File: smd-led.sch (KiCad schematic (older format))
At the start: 26 parts, among them Q14 Q_NPN_BEC, Q15 Q_NPN_BEC, Q17 Q_NPN_BEC, Q18 Q_NPN_BEC

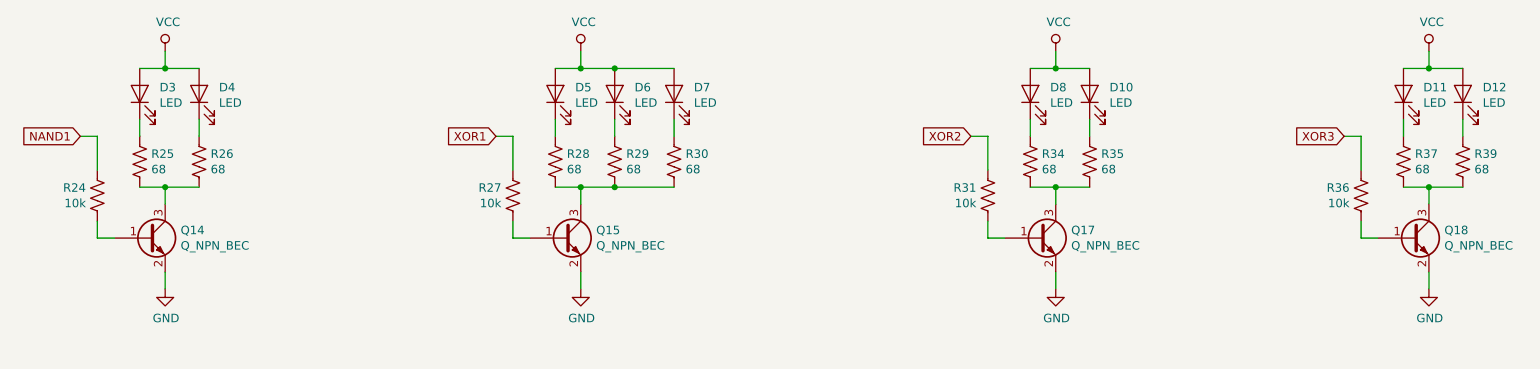
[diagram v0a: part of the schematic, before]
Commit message: refactor numeric assignments
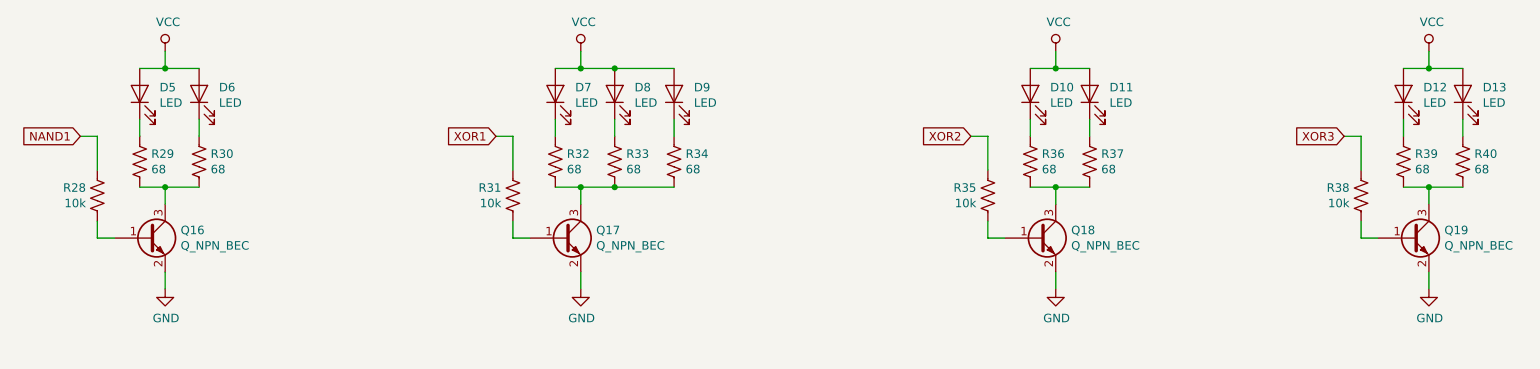
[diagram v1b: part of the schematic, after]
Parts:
- renumbered D8 to D10, D10 to D11, D11 to D12, D12 to D13, D3 to D5, D4 to D6, D5 to D7, D6 to D8, D7 to D9, Q14 to Q16, Q15 to Q17, Q17 to Q18, Q18 to Q19, R24 to R28, R25 to R29, R26 to R30, R27 to R31, R28 to R32, R29 to R33, R30 to R34, R31 to R35, R34 to R36, R35 to R37, R36 to R38, R37 to R39, R39 to R40
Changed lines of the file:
@@
 $EndDescr
 $Comp
-L Device:LED D3
+L Device:LED D5
 U 1 1 5CFFBE87
 P 1950 1500
-F 0 "D3" V 1988 1383 50  0000 R CNN
+F 0 "D5" V 1988 1383 50  0000 R CNN
 F 1 "LED" V 1897 1383 50  0000 R CNN
 F 2 "--Project:LED_1206_3216Metric_ReverseMount_Hole1.8x2.4mm" H 1950 1500 50  0001 C CNN
@@
 $EndComp
 $Comp
-L Device:R_US R25
+L Device:R_US R29
 U 1 1 5CFFBE8E
 P 1950 1900
-F 0 "R25" H 2018 1946 50  0000 L CNN
+F 0 "R29" H 2018 1946 50  0000 L CNN
 F 1 "68" H 2018 1855 50  0000 L CNN
 F 2 "Resistor_SMD:R_0805_2012Metric_Pad1.15x1.40mm_HandSolder" V 1990 1890 50  0001 C CNN
@@
 $EndComp
 $Comp
-L power:GND #PWR02
+L power:GND #PWR028
 U 1 1 5CFFBE95
 P 2100 2650
-F 0 "#PWR02" H 2100 2400 50  0001 C CNN
+F 0 "#PWR028" H 2100 2400 50  0001 C CNN
 F 1 "GND" H 2105 2477 50  0000 C CNN
 F 2 "" H 2100 2650 50  0001 C CNN
@@
 	1950 1750 1950 1650
 $Comp
-L power:VCC #PWR01
+L power:VCC #PWR027
 U 1 1 5CFFBE9D
 P 2100 1250
-F 0 "#PWR01" H 2100 1100 50  0001 C CNN
+F 0 "#PWR027" H 2100 1100 50  0001 C CNN
 F 1 "VCC" H 2117 1423 50  0000 C CNN
 F 2 "" H 2100 1250 50  0001 C CNN
@@
 	2100 1250 2100 1350
 $Comp
-L Device:R_US R24
+L Device:R_US R28
 U 1 1 5CFFBEA4
 P 1700 2100
-F 0 "R24" H 1767 2054 50  0000 L CNN
+F 0 "R28" H 1767 2054 50  0000 L CNN
 F 1 "10k" H 1767 2145 50  0000 L CNN
 F 2 "Resistor_SMD:R_0805_2012Metric_Pad1.15x1.40mm_HandSolder" V 1740 2090 50  0001 C CNN
@@
 	1600 1750 1700 1750
 $Comp
-L Device:LED D4
+L Device:LED D6
 U 1 1 5CFFBEB2
 P 2300 1500
-F 0 "D4" V 2338 1383 50  0000 R CNN
+F 0 "D6" V 2338 1383 50  0000 R CNN
 F 1 "LED" V 2247 1383 50  0000 R CNN
 F 2 "--Project:LED_1206_3216Metric_ReverseMount_Hole1.8x2.4mm" H 2300 1500 50  0001 C CNN
@@
 $EndComp
 $Comp
-L Device:R_US R26
+L Device:R_US R30
 U 1 1 5CFFBEB9
 P 2300 1900
-F 0 "R26" H 2368 1946 50  0000 L CNN
+F 0 "R30" H 2368 1946 50  0000 L CNN
 F 1 "68" H 2368 1855 50  0000 L CNN
 F 2 "Resistor_SMD:R_0805_2012Metric_Pad1.15x1.40mm_HandSolder" V 2340 1890 50  0001 C CNN
@@
 	2100 1350 2300 1350
 $Comp
-L Device:LED D8
+L Device:LED D10
 U 1 1 5CFFBEC8
 P 7200 1500
-F 0 "D8" V 7238 1383 50  0000 R CNN
+F 0 "D10" V 7238 1383 50  0000 R CNN
 F 1 "LED" V 7147 1383 50  0000 R CNN
 F 2 "--Project:LED_1206_3216Metric_ReverseMount_Hole1.8x2.4mm" H 7200 1500 50  0001 C CNN
@@
 $EndComp
 $Comp
-L Device:R_US R34
+L Device:R_US R36
 U 1 1 5CFFBECF
 P 7200 1900
-F 0 "R34" H 7268 1946 50  0000 L CNN
+F 0 "R36" H 7268 1946 50  0000 L CNN
 F 1 "68" H 7268 1855 50  0000 L CNN
 F 2 "Resistor_SMD:R_0805_2012Metric_Pad1.15x1.40mm_HandSolder" V 7240 1890 50  0001 C CNN
@@
 $EndComp
 $Comp
-L power:GND #PWR07
+L power:GND #PWR032
 U 1 1 5CFFBED6
 P 7350 2650
-F 0 "#PWR07" H 7350 2400 50  0001 C CNN
+F 0 "#PWR032" H 7350 2400 50  0001 C CNN
 F 1 "GND" H 7355 2477 50  0000 C CNN
 F 2 "" H 7350 2650 50  0001 C CNN
@@
 	7200 1750 7200 1650
 $Comp
-L power:VCC #PWR06
+L power:VCC #PWR031
 U 1 1 5CFFBEDE
 P 7350 1250
-F 0 "#PWR06" H 7350 1100 50  0001 C CNN
+F 0 "#PWR031" H 7350 1100 50  0001 C CNN
 F 1 "VCC" H 7367 1423 50  0000 C CNN
 F 2 "" H 7350 1250 50  0001 C CNN
@@
 	7350 1250 7350 1350
 $Comp
-L Device:R_US R31
+L Device:R_US R35
 U 1 1 5CFFBEE5
 P 6950 2100
-F 0 "R31" H 7018 2054 50  0000 L CNN
+F 0 "R35" H 7018 2054 50  0000 L CNN
 F 1 "10k" H 7018 2145 50  0000 L CNN
 F 2 "Resistor_SMD:R_0805_2012Metric_Pad1.15x1.40mm_HandSolder" V 6990 2090 50  0001 C CNN
@@
 	6850 1750 6950 1750
 $Comp
-L Device:LED D10
+L Device:LED D11
 U 1 1 5CFFBEF3
 P 7550 1500
-F 0 "D10" V 7588 1383 50  0000 R CNN
+F 0 "D11" V 7588 1383 50  0000 R CNN
 F 1 "LED" V 7497 1383 50  0000 R CNN
 F 2 "--Project:LED_1206_3216Metric_ReverseMount_Hole1.8x2.4mm" H 7550 1500 50  0001 C CNN
@@
 $EndComp
 $Comp
-L Device:R_US R35
+L Device:R_US R37
 U 1 1 5CFFBEFA
 P 7550 1900
-F 0 "R35" H 7618 1946 50  0000 L CNN
+F 0 "R37" H 7618 1946 50  0000 L CNN
 F 1 "68" H 7618 1855 50  0000 L CNN
 F 2 "Resistor_SMD:R_0805_2012Metric_Pad1.15x1.40mm_HandSolder" V 7590 1890 50  0001 C CNN
@@
 	7350 1350 7550 1350
 $Comp
-L Device:LED D11
+L Device:LED D12
 U 1 1 5CFFBF09
 P 9400 1500
-F 0 "D11" V 9438 1383 50  0000 R CNN
+F 0 "D12" V 9438 1383 50  0000 R CNN
 F 1 "LED" V 9347 1383 50  0000 R CNN
 F 2 "--Project:LED_1206_3216Metric_ReverseMount_Hole1.8x2.4mm" H 9400 1500 50  0001 C CNN
@@
 $EndComp
 $Comp
-L Device:R_US R37
+L Device:R_US R39
 U 1 1 5CFFBF10
 P 9400 1900
-F 0 "R37" H 9468 1946 50  0000 L CNN
+F 0 "R39" H 9468 1946 50  0000 L CNN
 F 1 "68" H 9468 1855 50  0000 L CNN
 F 2 "Resistor_SMD:R_0805_2012Metric_Pad1.15x1.40mm_HandSolder" V 9440 1890 50  0001 C CNN
@@
 $EndComp
 $Comp
-L power:GND #PWR09
+L power:GND #PWR034
 U 1 1 5CFFBF17
 P 9550 2650
-F 0 "#PWR09" H 9550 2400 50  0001 C CNN
+F 0 "#PWR034" H 9550 2400 50  0001 C CNN
 F 1 "GND" H 9555 2477 50  0000 C CNN
 F 2 "" H 9550 2650 50  0001 C CNN
@@
 	9400 1750 9400 1650
 $Comp
-L power:VCC #PWR08
+L power:VCC #PWR033
 U 1 1 5CFFBF1F
 P 9550 1250
-F 0 "#PWR08" H 9550 1100 50  0001 C CNN
+F 0 "#PWR033" H 9550 1100 50  0001 C CNN
 F 1 "VCC" H 9567 1423 50  0000 C CNN
 F 2 "" H 9550 1250 50  0001 C CNN
@@
 	9550 1250 9550 1350
 $Comp
-L Device:R_US R36
+L Device:R_US R38
 U 1 1 5CFFBF26
 P 9150 2100
-F 0 "R36" H 9218 2054 50  0000 L CNN
+F 0 "R38" H 9218 2054 50  0000 L CNN
 F 1 "10k" H 9218 2145 50  0000 L CNN
 F 2 "Resistor_SMD:R_0805_2012Metric_Pad1.15x1.40mm_HandSolder" V 9190 2090 50  0001 C CNN
@@
 	9050 1750 9150 1750
 $Comp
-L Device:LED D12
+L Device:LED D13
 U 1 1 5CFFBF34
 P 9750 1500
-F 0 "D12" V 9788 1383 50  0000 R CNN
+F 0 "D13" V 9788 1383 50  0000 R CNN
 F 1 "LED" V 9697 1383 50  0000 R CNN
 F 2 "--Project:LED_1206_3216Metric_ReverseMount_Hole1.8x2.4mm" H 9750 1500 50  0001 C CNN
@@
 $EndComp
 $Comp
-L Device:R_US R39
+L Device:R_US R40
 U 1 1 5CFFBF3B
 P 9750 1900
-F 0 "R39" H 9818 1946 50  0000 L CNN
+F 0 "R40" H 9818 1946 50  0000 L CNN
 F 1 "68" H 9818 1855 50  0000 L CNN
 F 2 "Resistor_SMD:R_0805_2012Metric_Pad1.15x1.40mm_HandSolder" V 9790 1890 50  0001 C CNN
@@
 	9550 1350 9750 1350
 $Comp
-L Device:LED D5
+L Device:LED D7
 U 1 1 5CFFBF4A
 P 4400 1500
-F 0 "D5" V 4438 1383 50  0000 R CNN
+F 0 "D7" V 4438 1383 50  0000 R CNN
 F 1 "LED" V 4347 1383 50  0000 R CNN
 F 2 "--Project:LED_1206_3216Metric_ReverseMount_Hole1.8x2.4mm" H 4400 1500 50  0001 C CNN
@@
 $EndComp
 $Comp
-L Device:R_US R28
+L Device:R_US R32
 U 1 1 5CFFBF51
 P 4400 1900
-F 0 "R28" H 4468 1946 50  0000 L CNN
+F 0 "R32" H 4468 1946 50  0000 L CNN
 F 1 "68" H 4468 1855 50  0000 L CNN
 F 2 "Resistor_SMD:R_0805_2012Metric_Pad1.15x1.40mm_HandSolder" V 4440 1890 50  0001 C CNN
@@
 $EndComp
 $Comp
-L power:GND #PWR04
+L power:GND #PWR030
 U 1 1 5CFFBF58
 P 4550 2650
-F 0 "#PWR04" H 4550 2400 50  0001 C CNN
+F 0 "#PWR030" H 4550 2400 50  0001 C CNN
 F 1 "GND" H 4555 2477 50  0000 C CNN
 F 2 "" H 4550 2650 50  0001 C CNN
@@
 	4400 1750 4400 1650
 $Comp
-L power:VCC #PWR03
+L power:VCC #PWR029
 U 1 1 5CFFBF60
 P 4550 1250
-F 0 "#PWR03" H 4550 1100 50  0001 C CNN
+F 0 "#PWR029" H 4550 1100 50  0001 C CNN
 F 1 "VCC" H 4567 1423 50  0000 C CNN
 F 2 "" H 4550 1250 50  0001 C CNN
@@
 	4550 1250 4550 1350
 $Comp
-L Device:R_US R27
+L Device:R_US R31
 U 1 1 5CFFBF67
 P 4150 2100
-F 0 "R27" H 4218 2054 50  0000 L CNN
+F 0 "R31" H 4218 2054 50  0000 L CNN
 F 1 "10k" H 4218 2145 50  0000 L CNN
 F 2 "Resistor_SMD:R_0805_2012Metric_Pad1.15x1.40mm_HandSolder" V 4190 2090 50  0001 C CNN
@@
 	4050 1750 4150 1750
 $Comp
-L Device:LED D6
+L Device:LED D8
 U 1 1 5CFFBF75
 P 4750 1500
-F 0 "D6" V 4788 1383 50  0000 R CNN
+F 0 "D8" V 4788 1383 50  0000 R CNN
 F 1 "LED" V 4697 1383 50  0000 R CNN
 F 2 "--Project:LED_1206_3216Metric_ReverseMount_Hole1.8x2.4mm" H 4750 1500 50  0001 C CNN
@@
 $EndComp
 $Comp
-L Device:R_US R29
+L Device:R_US R33
 U 1 1 5CFFBF7C
 P 4750 1900
-F 0 "R29" H 4818 1946 50  0000 L CNN
+F 0 "R33" H 4818 1946 50  0000 L CNN
 F 1 "68" H 4818 1855 50  0000 L CNN
 F 2 "Resistor_SMD:R_0805_2012Metric_Pad1.15x1.40mm_HandSolder" V 4790 1890 50  0001 C CNN
@@
 	4750 1750 4750 1650
 $Comp
-L Device:LED D7
+L Device:LED D9
 U 1 1 5CFFBF85
 P 5100 1500
-F 0 "D7" V 5138 1383 50  0000 R CNN
+F 0 "D9" V 5138 1383 50  0000 R CNN
 F 1 "LED" V 5047 1383 50  0000 R CNN
 F 2 "--Project:LED_1206_3216Metric_ReverseMount_Hole1.8x2.4mm" H 5100 1500 50  0001 C CNN
@@
 $EndComp
 $Comp
-L Device:R_US R30
+L Device:R_US R34
 U 1 1 5CFFBF8C
 P 5100 1900
-F 0 "R30" H 5168 1946 50  0000 L CNN
+F 0 "R34" H 5168 1946 50  0000 L CNN
 F 1 "68" H 5168 1855 50  0000 L CNN
 F 2 "Resistor_SMD:R_0805_2012Metric_Pad1.15x1.40mm_HandSolder" V 5140 1890 50  0001 C CNN
@@
 	4750 1350 5100 1350
 $Comp
-L Device:Q_NPN_BEC Q14
+L Device:Q_NPN_BEC Q16
 U 1 1 5CFFBF9F
 P 2000 2350
-F 0 "Q14" H 2191 2396 50  0000 L CNN
+F 0 "Q16" H 2191 2396 50  0000 L CNN
 F 1 "Q_NPN_BEC" H 2191 2305 50  0000 L CNN
 F 2 "Package_TO_SOT_SMD:SOT-23_Handsoldering" H 2200 2450 50  0001 C CNN
@@
 $EndComp
 $Comp
-L Device:Q_NPN_BEC Q17
+L Device:Q_NPN_BEC Q18
 U 1 1 5CFFBFA7
 P 7250 2350
-F 0 "Q17" H 7441 2396 50  0000 L CNN
+F 0 "Q18" H 7441 2396 50  0000 L CNN
 F 1 "Q_NPN_BEC" H 7441 2305 50  0000 L CNN
 F 2 "Package_TO_SOT_SMD:SOT-23_Handsoldering" H 7450 2450 50  0001 C CNN
@@
 $EndComp
 $Comp
-L Device:Q_NPN_BEC Q18
+L Device:Q_NPN_BEC Q19
 U 1 1 5CFFBFAF
 P 9450 2350
-F 0 "Q18" H 9641 2396 50  0000 L CNN
+F 0 "Q19" H 9641 2396 50  0000 L CNN
 F 1 "Q_NPN_BEC" H 9641 2305 50  0000 L CNN
 F 2 "Package_TO_SOT_SMD:SOT-23_Handsoldering" H 9650 2450 50  0001 C CNN
@@
 $EndComp
 $Comp
-L Device:Q_NPN_BEC Q15
+L Device:Q_NPN_BEC Q17
 U 1 1 5CFFBFB7
 P 4450 2350
-F 0 "Q15" H 4641 2396 50  0000 L CNN
+F 0 "Q17" H 4641 2396 50  0000 L CNN
 F 1 "Q_NPN_BEC" H 4641 2305 50  0000 L CNN
 F 2 "Package_TO_SOT_SMD:SOT-23_Handsoldering" H 4650 2450 50  0001 C CNN

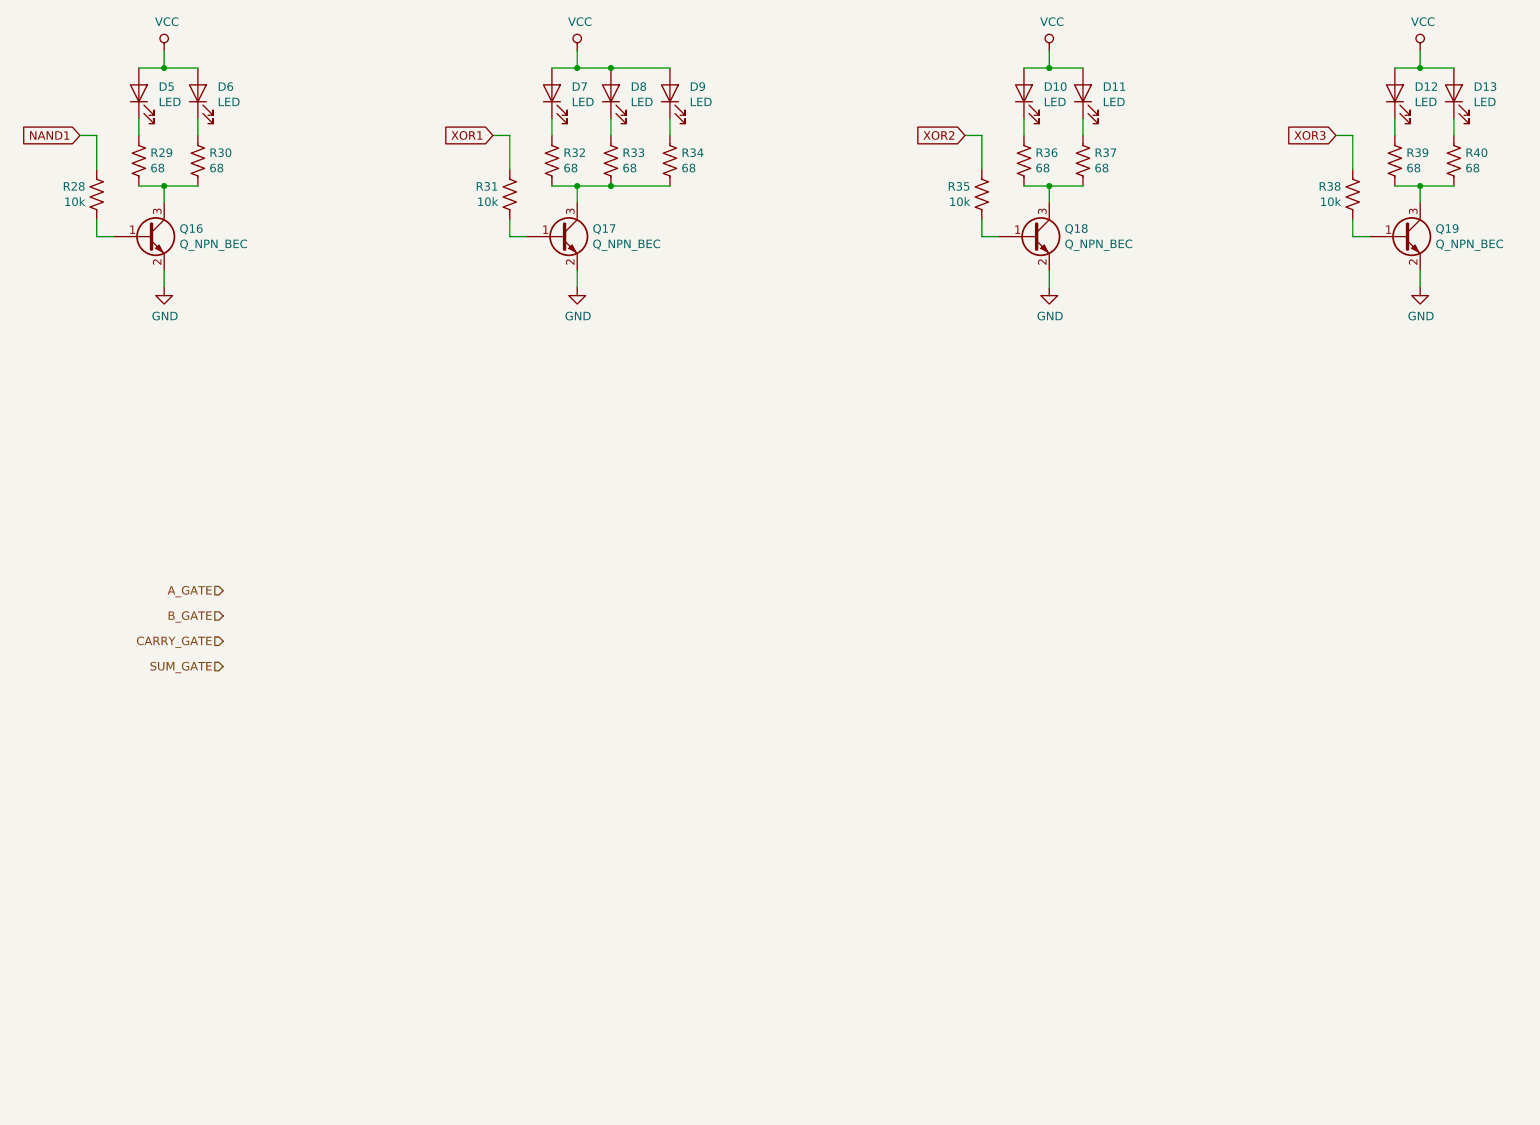
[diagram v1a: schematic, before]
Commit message: full smd led array layout done
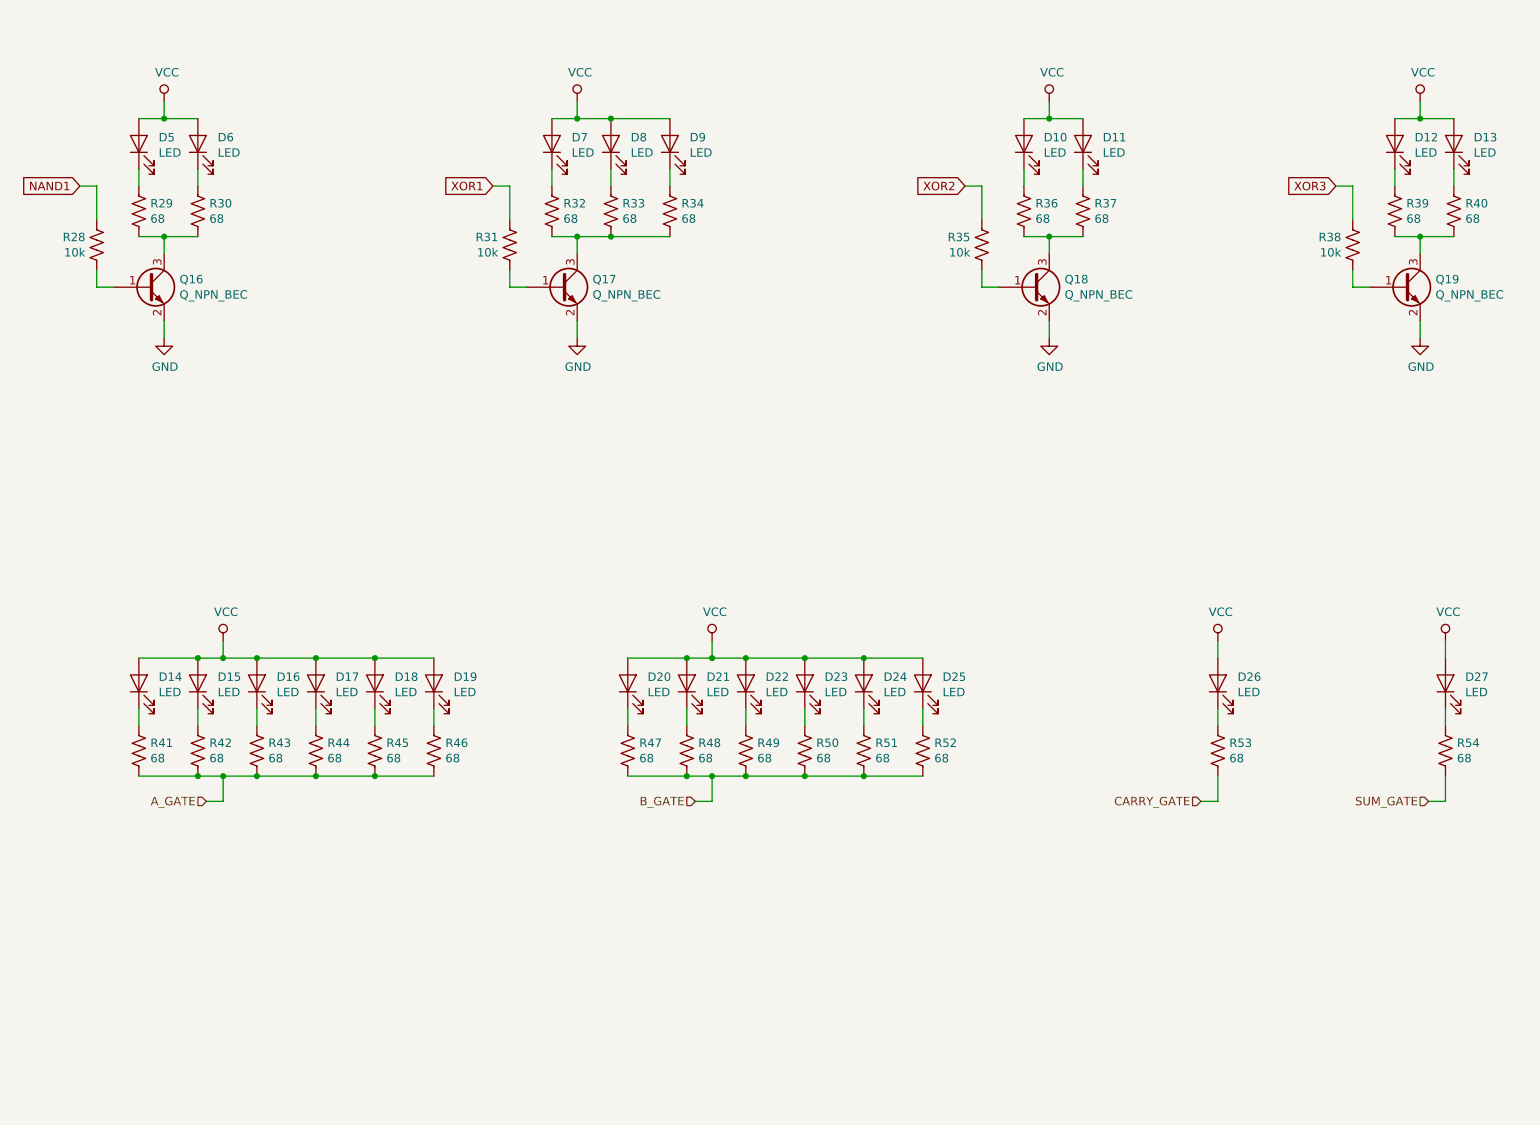
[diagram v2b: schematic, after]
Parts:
- added D14, D15, D16, D17, D18, D19, D20, D21, D22, D23, D24, D25, D26, D27: LED, --Project:LED_1206_3216Metric_ReverseMount_Hole1.8x2.4mm, symbol Device:LED
- added R41, R42, R43, R44, R45, R46, R47, R48, R49, R50, R51, R52, R53, R54: 68, Resistor_SMD:R_0805_2012Metric_Pad1.15x1.40mm_HandSolder, symbol Device:R_US
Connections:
- net A_GATE: now also R41.2, R42.2, R43.2, R44.2, R45.2, R46.2
- net B_GATE: now also R47.2, R48.2, R49.2, R50.2, R51.2, R52.2
- net CARRY_GATE: now also R53.2
- net SUM_GATE: now also R54.2
- net VCC: now also D14.2 (A), D15.2 (A), D16.2 (A), D17.2 (A), D18.2 (A), D19.2 (A), D20.2 (A), D21.2 (A), D22.2 (A), D23.2 (A), D24.2 (A), D25.2 (A), D26.2 (A), D27.2 (A)
- new net: D14.1 (K), R41.1
- new net: D15.1 (K), R42.1
- new net: D16.1 (K), R43.1
- new net: D17.1 (K), R44.1
- new net: D18.1 (K), R45.1
- new net: D19.1 (K), R46.1
- new net: D20.1 (K), R47.1
- new net: D21.1 (K), R48.1
- new net: D22.1 (K), R49.1
- new net: D23.1 (K), R50.1
- new net: D24.1 (K), R51.1
- new net: D25.1 (K), R52.1
- new net: D26.1 (K), R53.1
- new net: D27.1 (K), R54.1
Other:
- moved on the sheet: D10, D11, D12, D13, D5, D6, D7, D8, D9, Q16, Q17, Q18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

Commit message: add sheet annotations
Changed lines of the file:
@@
 encoding utf-8
 Sheet 2 2
-Title ""
-Date ""
-Rev ""
+Title "RTL Half Adder"
+Date "2019-06-12"
+Rev "v1"
 Comp ""
-Comment1 ""
-Comment2 ""
-Comment3 ""
-Comment4 ""
+Comment1 "creativecommons.org/licenses/by-nc-sa/4.0/"
+Comment2 "CC BY-NC-SA"
+Comment3 "github.com/tyehle/rtl-half-adder"
+Comment4 "Author: Tobin Yehle"
 $EndDescr
 $Comp
@@
 Wire Wire Line
 	9700 5700 9700 5550
+$Comp
+L Graphic:Logo_Open_Hardware_Large #LOGO?
+U 1 1 5D036C9E
+P 6350 7200
+F 0 "#LOGO?" H 6350 7700 50  0001 C CNN
+F 1 "Logo_Open_Hardware_Large" H 6350 6800 50  0001 C CNN
+F 2 "" H 6350 7200 50  0001 C CNN
+F 3 "~" H 6350 7200 50  0001 C CNN
+	1    6350 7200
+	1    0    0    -1
+$EndComp
 $EndSCHEMATC

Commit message: change led footprint
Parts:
- D10, D11, D12, D13, D14, D15, D16, D17, D18, D19, D20, D21, D22, D23, D24, D25, D26, D27, D5, D6, D7, D8, D9: footprint --Project:LED_1206_3216Metric_ReverseMount_Hole1.8x2.4mm -> --Project:LED_1206_ReverseMountSquare1.5mm_HandSolder
